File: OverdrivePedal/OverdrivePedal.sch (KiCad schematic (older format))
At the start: 12 parts, among them J1 Conn_01x02, J2 Conn_01x02, J3 Conn_01x03, J4 Conn_01x03, J5 Conn_01x03, J6 Conn_01x02, U1 TL071

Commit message: RevA Layout completed
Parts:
- C1: footprint Capacitor_SMD:C_1206_3216Metric_Pad1.42x1.75mm_HandSolder -> Capacitor_SMD:C_0805_2012Metric_Pad1.15x1.40mm_HandSolder
- R1, R2, R3: footprint Resistor_SMD:R_1206_3216Metric_Pad1.42x1.75mm_HandSolder -> Resistor_SMD:R_0805_2012Metric_Pad1.15x1.40mm_HandSolder
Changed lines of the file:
@@
 F 0 "R2" H 5470 4196 50  0000 L CNN
 F 1 "2K7" H 5470 4105 50  0000 L CNN
-F 2 "Resistor_SMD:R_1206_3216Metric_Pad1.42x1.75mm_HandSolder" V 5330 4150 50  0001 C CNN
+F 2 "Resistor_SMD:R_0805_2012Metric_Pad1.15x1.40mm_HandSolder" V 5330 4150 50  0001 C CNN
 F 3 "~" H 5400 4150 50  0001 C CNN
 	1    5400 4150
@@
 F 0 "R3" H 8120 3646 50  0000 L CNN
 F 1 "10K" H 8120 3555 50  0000 L CNN
-F 2 "Resistor_SMD:R_1206_3216Metric_Pad1.42x1.75mm_HandSolder" V 7980 3600 50  0001 C CNN
+F 2 "Resistor_SMD:R_0805_2012Metric_Pad1.15x1.40mm_HandSolder" V 7980 3600 50  0001 C CNN
 F 3 "~" H 8050 3600 50  0001 C CNN
 	1    8050 3600
@@
 F 0 "R1" H 4420 3646 50  0000 L CNN
 F 1 "22M" H 4420 3555 50  0000 L CNN
-F 2 "Resistor_SMD:R_1206_3216Metric_Pad1.42x1.75mm_HandSolder" V 4280 3600 50  0001 C CNN
+F 2 "Resistor_SMD:R_0805_2012Metric_Pad1.15x1.40mm_HandSolder" V 4280 3600 50  0001 C CNN
 F 3 "~" H 4350 3600 50  0001 C CNN
 	1    4350 3600
@@
 F 0 "C1" V 4000 2700 50  0000 L CNN
 F 1 "100nF" V 3600 2650 50  0000 L CNN
-F 2 "Capacitor_SMD:C_1206_3216Metric_Pad1.42x1.75mm_HandSolder" H 3838 2600 50  0001 C CNN
+F 2 "Capacitor_SMD:C_0805_2012Metric_Pad1.15x1.40mm_HandSolder" H 3838 2600 50  0001 C CNN
 F 3 "~" H 3800 2750 50  0001 C CNN
 	1    3800 2750

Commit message: Replaced TL071 with TL072
UPDATED LAYOUT
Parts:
- removed U1: TL071, Package_SO:SOIC-8_3.9x4.9mm_P1.27mm, symbol Amplifier_Operational:TL071
- added U1: TL072, Package_SO:SOIC-8_3.9x4.9mm_P1.27mm, symbol Amplifier_Operational:TL072
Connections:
- wire segments 49 -> 55
- no-connect marks 2 -> 0
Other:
- moved on the sheet: C1, J2, R1
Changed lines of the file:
@@
 $EndDescr
-$Comp
-L Amplifier_Operational:TL071 U1
-U 1 1 5E5FD495
-P 6000 2850
-F 0 "U1" H 6250 3200 50  0000 L CNN
-F 1 "TL071" H 6200 3100 50  0000 L CNN
-F 2 "Package_SO:SOIC-8_3.9x4.9mm_P1.27mm" H 6050 2900 50  0001 C CNN
-F 3 "http://www.ti.com/lit/ds/symlink/tl071.pdf" H 6150 3000 50  0001 C CNN
-	1    6000 2850
-	1    0    0    -1
-$EndComp
 $Comp
 L Connector_Generic:Conn_01x03 J4
@@
 	6750 2850 6300 2850
 Wire Wire Line
-	5900 3150 5900 3300
-$Comp
-L power:-5V #PWR08
-U 1 1 5E601192
-P 5900 3300
-F 0 "#PWR08" H 5900 3400 50  0001 C CNN
-F 1 "-5V" H 5915 3473 50  0000 C CNN
-F 2 "" H 5900 3300 50  0001 C CNN
-F 3 "" H 5900 3300 50  0001 C CNN
-	1    5900 3300
-	-1   0    0    1
-$EndComp
-$Comp
-L power:+5V #PWR07
-U 1 1 5E60134C
-P 5900 2400
-F 0 "#PWR07" H 5900 2250 50  0001 C CNN
-F 1 "+5V" H 5915 2573 50  0000 C CNN
-F 2 "" H 5900 2400 50  0001 C CNN
-F 3 "" H 5900 2400 50  0001 C CNN
-	1    5900 2400
-	1    0    0    -1
-$EndComp
-Wire Wire Line
-	5900 2400 5900 2550
-NoConn ~ 6000 3150
-NoConn ~ 6100 3150
-Wire Wire Line
 	6000 3800 6000 3600
 Wire Wire Line
@@
 $EndComp
 $Sheet
-S 3200 5950 1900 950
+S 2450 5900 1900 950
 U 5E6165F4
 F0 "PosNeg5V_PSU" 50
 F1 "PosNeg5V_PSU.sch" 50
-F2 "+9V_IN" I L 3200 6200 50
-F3 "+5V" I R 5100 6250 50
-F4 "-5V" I R 5100 6500 50
+F2 "+9V_IN" I L 2450 6150 50
+F3 "+5V" I R 4350 6200 50
+F4 "-5V" I R 4350 6450 50
 $EndSheet
 Wire Wire Line
-	5100 6250 5450 6250
-Wire Wire Line
-	5450 6250 5450 5950
+	4350 6200 4700 6200
+Wire Wire Line
+	4700 6200 4700 5900
 $Comp
 L power:+5V #PWR04
 U 1 1 5E668A6B
-P 5450 5950
-F 0 "#PWR04" H 5450 5800 50  0001 C CNN
-F 1 "+5V" H 5465 6123 50  0000 C CNN
-F 2 "" H 5450 5950 50  0001 C CNN
-F 3 "" H 5450 5950 50  0001 C CNN
-	1    5450 5950
+P 4700 5900
+F 0 "#PWR04" H 4700 5750 50  0001 C CNN
+F 1 "+5V" H 4715 6073 50  0000 C CNN
+F 2 "" H 4700 5900 50  0001 C CNN
+F 3 "" H 4700 5900 50  0001 C CNN
+	1    4700 5900
 	1    0    0    -1
 $EndComp
@@
 L power:-5V #PWR05
 U 1 1 5E668F99
-P 5450 6700
-F 0 "#PWR05" H 5450 6800 50  0001 C CNN
-F 1 "-5V" H 5465 6873 50  0000 C CNN
-F 2 "" H 5450 6700 50  0001 C CNN
-F 3 "" H 5450 6700 50  0001 C CNN
-	1    5450 6700
+P 4700 6650
+F 0 "#PWR05" H 4700 6750 50  0001 C CNN
+F 1 "-5V" H 4715 6823 50  0000 C CNN
+F 2 "" H 4700 6650 50  0001 C CNN
+F 3 "" H 4700 6650 50  0001 C CNN
+	1    4700 6650
 	-1   0    0    1
 $EndComp
 Wire Wire Line
-	5100 6500 5450 6500
-Wire Wire Line
-	5450 6500 5450 6700
-Wire Wire Line
-	3200 6200 2200 6200
+	4350 6450 4700 6450
+Wire Wire Line
+	4700 6450 4700 6650
+Wire Wire Line
+	2450 6150 1450 6150
 $Comp
 L Connector_Generic:Conn_01x02 J2
 U 1 1 5E669F6B
-P 2000 6200
-F 0 "J2" H 1918 6417 50  0000 C CNN
-F 1 "Conn_01x02" H 1918 6326 50  0000 C CNN
-F 2 "Connector_PinHeader_2.54mm:PinHeader_1x02_P2.54mm_Vertical" H 2000 6200 50  0001 C CNN
-F 3 "~" H 2000 6200 50  0001 C CNN
-	1    2000 6200
+P 1250 6150
+F 0 "J2" H 1168 6367 50  0000 C CNN
+F 1 "Conn_01x02" H 1168 6276 50  0000 C CNN
+F 2 "Connector_PinHeader_2.54mm:PinHeader_1x02_P2.54mm_Vertical" H 1250 6150 50  0001 C CNN
+F 3 "~" H 1250 6150 50  0001 C CNN
+	1    1250 6150
 	-1   0    0    -1
 $EndComp
 Wire Wire Line
-	2200 6300 2600 6300
-Wire Wire Line
-	2600 6300 2600 6800
+	1450 6250 1850 6250
+Wire Wire Line
+	1850 6250 1850 6750
 $Comp
 L power:GNDS #PWR02
 U 1 1 5E66AC31
-P 2600 6800
-F 0 "#PWR02" H 2600 6550 50  0001 C CNN
-F 1 "GNDS" H 2605 6627 50  0000 C CNN
-F 2 "" H 2600 6800 50  0001 C CNN
-F 3 "" H 2600 6800 50  0001 C CNN
-	1    2600 6800
+P 1850 6750
+F 0 "#PWR02" H 1850 6500 50  0001 C CNN
+F 1 "GNDS" H 1855 6577 50  0000 C CNN
+F 2 "" H 1850 6750 50  0001 C CNN
+F 3 "" H 1850 6750 50  0001 C CNN
+	1    1850 6750
 	1    0    0    -1
 $EndComp
@@
 L Device:R R1
 U 1 1 5E66BD48
-P 4350 3600
-F 0 "R1" H 4420 3646 50  0000 L CNN
-F 1 "22M" H 4420 3555 50  0000 L CNN
-F 2 "Resistor_SMD:R_0805_2012Metric_Pad1.15x1.40mm_HandSolder" V 4280 3600 50  0001 C CNN
-F 3 "~" H 4350 3600 50  0001 C CNN
-	1    4350 3600
-	1    0    0    -1
-$EndComp
-Wire Wire Line
-	4350 3450 4350 2750
-Wire Wire Line
-	4350 2750 5700 2750
-Wire Wire Line
-	4350 3750 4350 4650
+P 3800 3500
+F 0 "R1" H 3870 3546 50  0000 L CNN
+F 1 "22M" H 3870 3455 50  0000 L CNN
+F 2 "Resistor_SMD:R_0805_2012Metric_Pad1.15x1.40mm_HandSolder" V 3730 3500 50  0001 C CNN
+F 3 "~" H 3800 3500 50  0001 C CNN
+	1    3800 3500
+	1    0    0    -1
+$EndComp
+Wire Wire Line
+	3800 3350 3800 2650
+Wire Wire Line
+	3800 2650 4300 2650
+Wire Wire Line
+	3800 3650 3800 4550
 $Comp
 L power:GNDS #PWR03
 U 1 1 5E66CC4B
-P 4350 4650
-F 0 "#PWR03" H 4350 4400 50  0001 C CNN
-F 1 "GNDS" H 4355 4477 50  0000 C CNN
-F 2 "" H 4350 4650 50  0001 C CNN
-F 3 "" H 4350 4650 50  0001 C CNN
-	1    4350 4650
+P 3800 4550
+F 0 "#PWR03" H 3800 4300 50  0001 C CNN
+F 1 "GNDS" H 3805 4377 50  0000 C CNN
+F 2 "" H 3800 4550 50  0001 C CNN
+F 3 "" H 3800 4550 50  0001 C CNN
+	1    3800 4550
 	1    0    0    -1
 $EndComp
@@
 Wire Wire Line
 	1700 2050 3000 2050
-Connection ~ 4350 2750
+Connection ~ 3800 2650
 $Comp
 L power:GND #PWR01
@@
 $EndComp
 Wire Wire Line
-	3950 2750 4350 2750
+	3400 2650 3800 2650
 $Comp
 L Device:C C?
 U 1 1 5E67DF73
-P 3800 2750
+P 3250 2650
 AR Path="/5E6165F4/5E67DF73" Ref="C?"  Part="1"
 AR Path="/5E67DF73" Ref="C1"  Part="1"
-F 0 "C1" V 4000 2700 50  0000 L CNN
-F 1 "100nF" V 3600 2650 50  0000 L CNN
-F 2 "Capacitor_SMD:C_0805_2012Metric_Pad1.15x1.40mm_HandSolder" H 3838 2600 50  0001 C CNN
-F 3 "~" H 3800 2750 50  0001 C CNN
-	1    3800 2750
+F 0 "C1" V 3450 2600 50  0000 L CNN
+F 1 "100nF" V 3050 2550 50  0000 L CNN
+F 2 "Capacitor_SMD:C_0805_2012Metric_Pad1.15x1.40mm_HandSolder" H 3288 2500 50  0001 C CNN
+F 3 "~" H 3250 2650 50  0001 C CNN
+	1    3250 2650
 	0    -1   -1   0
 $EndComp
@@
 	3000 2150 2750 2150
 Wire Wire Line
-	2750 2150 2750 2750
-Wire Wire Line
-	2750 2750 3650 2750
+	2750 2150 2750 2650
+Wire Wire Line
+	2750 2650 3100 2650
 Text Notes 1400 1700 0    50   ~ 0
 Output Jack
@@
 Wire Wire Line
 	2000 3800 2000 4000
+$Comp
+L Amplifier_Operational:TL072 U1
+U 1 1 5E645B4B
+P 4600 2750
+F 0 "U1" H 4600 3117 50  0000 C CNN
+F 1 "TL072" H 4600 3026 50  0000 C CNN
+F 2 "Package_SO:SOIC-8_3.9x4.9mm_P1.27mm" H 4600 2750 50  0001 C CNN
+F 3 "http://www.ti.com/lit/ds/symlink/tl071.pdf" H 4600 2750 50  0001 C CNN
+	1    4600 2750
+	1    0    0    -1
+$EndComp
+$Comp
+L Amplifier_Operational:TL072 U1
+U 2 1 5E646D18
+P 6000 2850
+F 0 "U1" H 6000 3217 50  0000 C CNN
+F 1 "TL072" H 6000 3126 50  0000 C CNN
+F 2 "Package_SO:SOIC-8_3.9x4.9mm_P1.27mm" H 6000 2850 50  0001 C CNN
+F 3 "http://www.ti.com/lit/ds/symlink/tl071.pdf" H 6000 2850 50  0001 C CNN
+	2    6000 2850
+	1    0    0    -1
+$EndComp
+$Comp
+L Amplifier_Operational:TL072 U1
+U 3 1 5E64953A
+P 6000 6300
+F 0 "U1" H 5958 6346 50  0000 L CNN
+F 1 "TL072" H 5958 6255 50  0000 L CNN
+F 2 "Package_SO:SOIC-8_3.9x4.9mm_P1.27mm" H 6000 6300 50  0001 C CNN
+F 3 "http://www.ti.com/lit/ds/symlink/tl071.pdf" H 6000 6300 50  0001 C CNN
+	3    6000 6300
+	1    0    0    -1
+$EndComp
+Wire Wire Line
+	5900 6000 5900 5700
+$Comp
+L power:+5V #PWR07
+U 1 1 5E654320
+P 5900 5700
+F 0 "#PWR07" H 5900 5550 50  0001 C CNN
+F 1 "+5V" H 5915 5873 50  0000 C CNN
+F 2 "" H 5900 5700 50  0001 C CNN
+F 3 "" H 5900 5700 50  0001 C CNN
+	1    5900 5700
+	1    0    0    -1
+$EndComp
+$Comp
+L power:-5V #PWR08
+U 1 1 5E65531A
+P 5900 6800
+F 0 "#PWR08" H 5900 6900 50  0001 C CNN
+F 1 "-5V" H 5915 6973 50  0000 C CNN
+F 2 "" H 5900 6800 50  0001 C CNN
+F 3 "" H 5900 6800 50  0001 C CNN
+	1    5900 6800
+	-1   0    0    1
+$EndComp
+Wire Wire Line
+	5900 6600 5900 6800
+Wire Wire Line
+	4900 2750 5050 2750
+Wire Wire Line
+	4300 2850 4150 2850
+Wire Wire Line
+	4150 2850 4150 3150
+Wire Wire Line
+	4150 3150 5050 3150
+Wire Wire Line
+	5050 3150 5050 2750
+Connection ~ 5050 2750
+Wire Wire Line
+	5050 2750 5700 2750
 $EndSCHEMATC

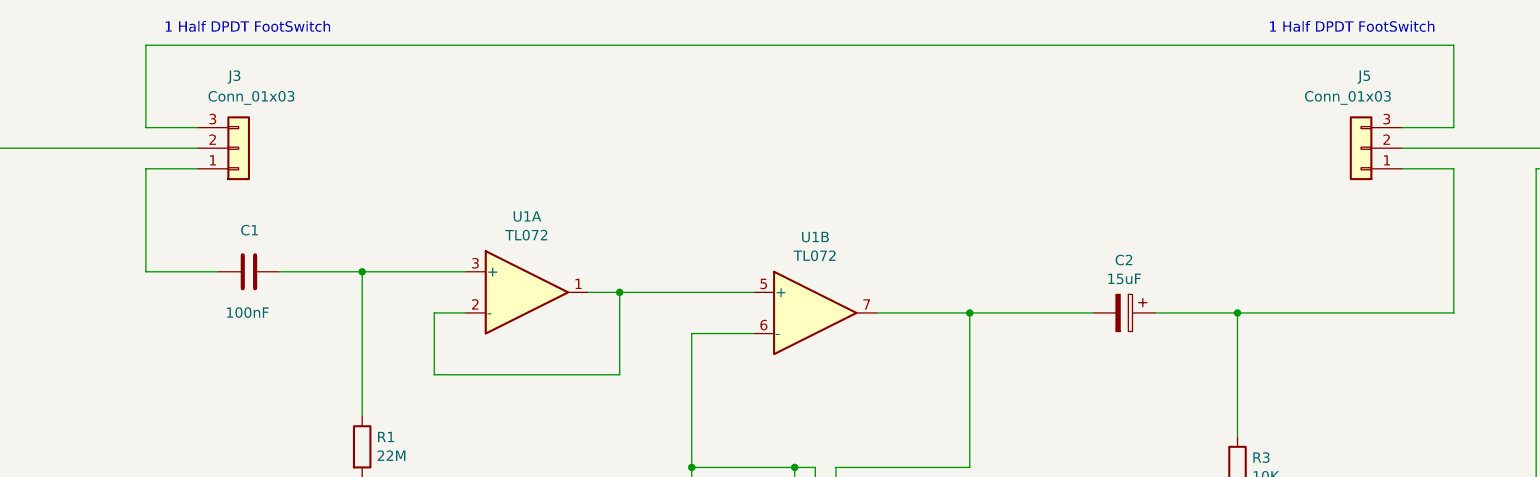
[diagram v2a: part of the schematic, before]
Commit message: Tested RevA Layout
- Removed AC coupling caps
- Reversed Switch connector
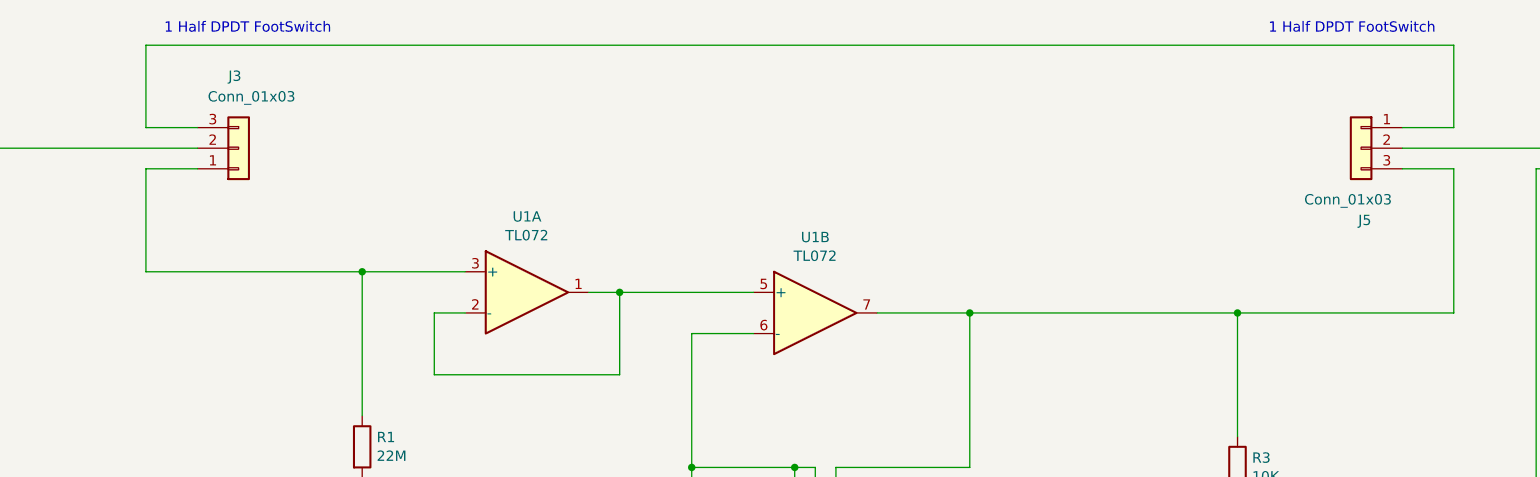
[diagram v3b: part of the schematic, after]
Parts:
- removed C1: 100nF, Capacitor_SMD:C_0805_2012Metric_Pad1.15x1.40mm_HandSolder, symbol Device:C
- removed C2: 15uF, Capacitor_SMD:CP_Elec_4x5.7, symbol Device:CP
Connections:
- net at J4.1 (Pin_1), U1.7: now also J5.3 (Pin_3), R3.1
- net at J5.1 (Pin_1): now also J3.3 (Pin_3); no longer R3.1
- net at R1.1, U1.3 (+): now also J3.1 (Pin_1)
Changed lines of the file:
@@
 	1    0    0    -1
 $EndComp
-$Comp
-L Device:CP C2
-U 1 1 5E603004
-P 7500 2850
-F 0 "C2" V 7245 2850 50  0000 C CNN
-F 1 "15uF" V 7336 2850 50  0000 C CNN
-F 2 "Capacitor_SMD:CP_Elec_4x5.7" H 7538 2700 50  0001 C CNN
-F 3 "~" H 7500 2850 50  0001 C CNN
-	1    7500 2850
-	0    1    1    0
-$EndComp
-Wire Wire Line
-	7350 2850 6750 2850
 Connection ~ 6750 2850
 $Comp
@@
 Wire Wire Line
 	8050 3450 8050 2850
-Wire Wire Line
-	8050 2850 7650 2850
 Wire Wire Line
 	8050 3750 8050 4650
@@
 	1    0    0    -1
 $EndComp
-Wire Wire Line
-	3400 2650 3800 2650
-$Comp
-L Device:C C?
-U 1 1 5E67DF73
-P 3250 2650
-AR Path="/5E6165F4/5E67DF73" Ref="C?"  Part="1"
-AR Path="/5E67DF73" Ref="C1"  Part="1"
-F 0 "C1" V 3450 2600 50  0000 L CNN
-F 1 "100nF" V 3050 2550 50  0000 L CNN
-F 2 "Capacitor_SMD:C_0805_2012Metric_Pad1.15x1.40mm_HandSolder" H 3288 2500 50  0001 C CNN
-F 3 "~" H 3250 2650 50  0001 C CNN
-	1    3250 2650
-	0    -1   -1   0
-$EndComp
 $Comp
 L Connector_Generic:Conn_01x03 J5
@@
 F 3 "~" H 8650 2050 50  0001 C CNN
 	1    8650 2050
-	-1   0    0    1
+	-1   0    0    -1
 $EndComp
 Wire Wire Line
@@
 Wire Wire Line
 	2750 2150 2750 2650
-Wire Wire Line
-	2750 2650 3100 2650
 Text Notes 1400 1700 0    50   ~ 0
 Output Jack
@@
 Wire Wire Line
 	5050 2750 5700 2750
+Wire Wire Line
+	2750 2650 3800 2650
+Wire Wire Line
+	6750 2850 8050 2850
 $EndSCHEMATC

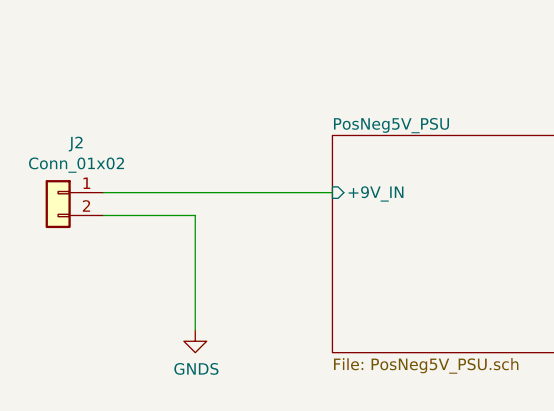
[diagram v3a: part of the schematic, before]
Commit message: changed polarity protection mosfet to schotky diode
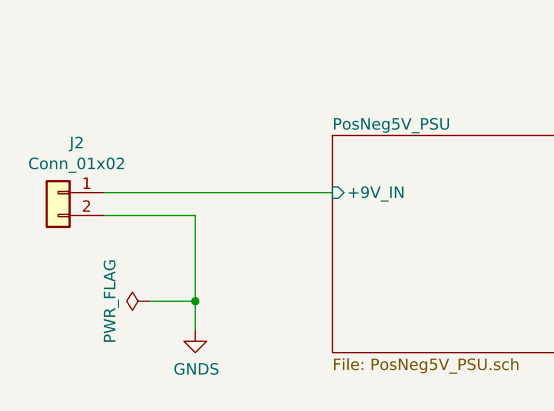
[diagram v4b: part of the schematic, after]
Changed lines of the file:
@@
 	1450 6250 1850 6250
 Wire Wire Line
-	1850 6250 1850 6750
+	1850 6250 1850 6625
 $Comp
 L power:GNDS #PWR02
@@
 Wire Wire Line
 	6750 2850 8050 2850
+$Comp
+L power:PWR_FLAG #FLG?
+U 1 1 5F657D2F
+P 1650 6625
+AR Path="/5E6165F4/5F657D2F" Ref="#FLG?"  Part="1"
+AR Path="/5F657D2F" Ref="#FLG0101"  Part="1"
+F 0 "#FLG0101" H 1650 6700 50  0001 C CNN
+F 1 "PWR_FLAG" H 1650 6798 50  0000 C CNN
+F 2 "" H 1650 6625 50  0001 C CNN
+F 3 "~" H 1650 6625 50  0001 C CNN
+	1    1650 6625
+	0    -1   -1   0
+$EndComp
+Wire Wire Line
+	1650 6625 1850 6625
+Connection ~ 1850 6625
+Wire Wire Line
+	1850 6625 1850 6750
 $EndSCHEMATC

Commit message: updates
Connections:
- net GND is gone; now on net GNDS: J1.2 (Pin_2)
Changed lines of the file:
@@
 	1700 2050 3000 2050
 Connection ~ 3800 2650
-$Comp
-L power:GND #PWR01
-U 1 1 5E6781D9
-P 2000 4000
-F 0 "#PWR01" H 2000 3750 50  0001 C CNN
-F 1 "GND" H 2005 3827 50  0000 C CNN
-F 2 "" H 2000 4000 50  0001 C CNN
-F 3 "" H 2000 4000 50  0001 C CNN
-	1    2000 4000
-	1    0    0    -1
-$EndComp
 Wire Wire Line
 	9600 2150 9500 2150
@@
 	1700 2150 2000 2150
 Wire Wire Line
-	2000 2150 2000 3800
-Wire Wire Line
 	3000 2150 2750 2150
 Wire Wire Line
@@
 Text Notes 1400 1700 0    50   ~ 0
 Output Jack
-$Comp
-L power:PWR_FLAG #FLG0103
-U 1 1 5E6CB28C
-P 2350 4000
-F 0 "#FLG0103" H 2350 4075 50  0001 C CNN
-F 1 "PWR_FLAG" H 2350 4173 50  0000 C CNN
-F 2 "" H 2350 4000 50  0001 C CNN
-F 3 "~" H 2350 4000 50  0001 C CNN
-	1    2350 4000
-	-1   0    0    1
-$EndComp
-Wire Wire Line
-	2350 4000 2350 3800
-Wire Wire Line
-	2350 3800 2000 3800
-Connection ~ 2000 3800
-Wire Wire Line
-	2000 3800 2000 4000
 $Comp
 L Amplifier_Operational:TL072 U1
@@
 Wire Wire Line
 	1850 6625 1850 6750
+$Comp
+L power:GNDS #PWR0101
+U 1 1 5F65FB73
+P 2000 4000
+F 0 "#PWR0101" H 2000 3750 50  0001 C CNN
+F 1 "GNDS" H 2005 3827 50  0000 C CNN
+F 2 "" H 2000 4000 50  0001 C CNN
+F 3 "" H 2000 4000 50  0001 C CNN
+	1    2000 4000
+	1    0    0    -1
+$EndComp
+Wire Wire Line
+	2000 2150 2000 4000
 $EndSCHEMATC
